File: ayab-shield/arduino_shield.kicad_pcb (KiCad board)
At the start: 2 copper layers, 73.1 x 53.3 mm, 36 parts, among them IC1 ULN2803A, IC2 ULN2803A, IC3 MCP2300X/P, IC4 MCP2300X/P, J1 Power, J2 Digital/PWM, J3 Analog, J4 Digital/PWM, X1 KLDX-0202-AC

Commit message: Gilding the lily
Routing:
- net GND: track 37.5 -> 16.6 mm, vias 2 -> 17
- net +15V: track 154.2 -> 138.8 mm
- net /SCL: track 111.9 -> 102.9 mm
- net /EOL_R: track 46.9 -> 39.5 mm
- net +5V: track 203.4 -> 198.6 mm, vias 0 -> 1
- net /ENC_A: track 25.9 -> 29.1 mm
- net /ENC_B: track 30.2 -> 28.3 mm
- net /SDA: track 95.1 -> 93.4 mm
- net /EOL_L: track 30.2 -> 29.2 mm

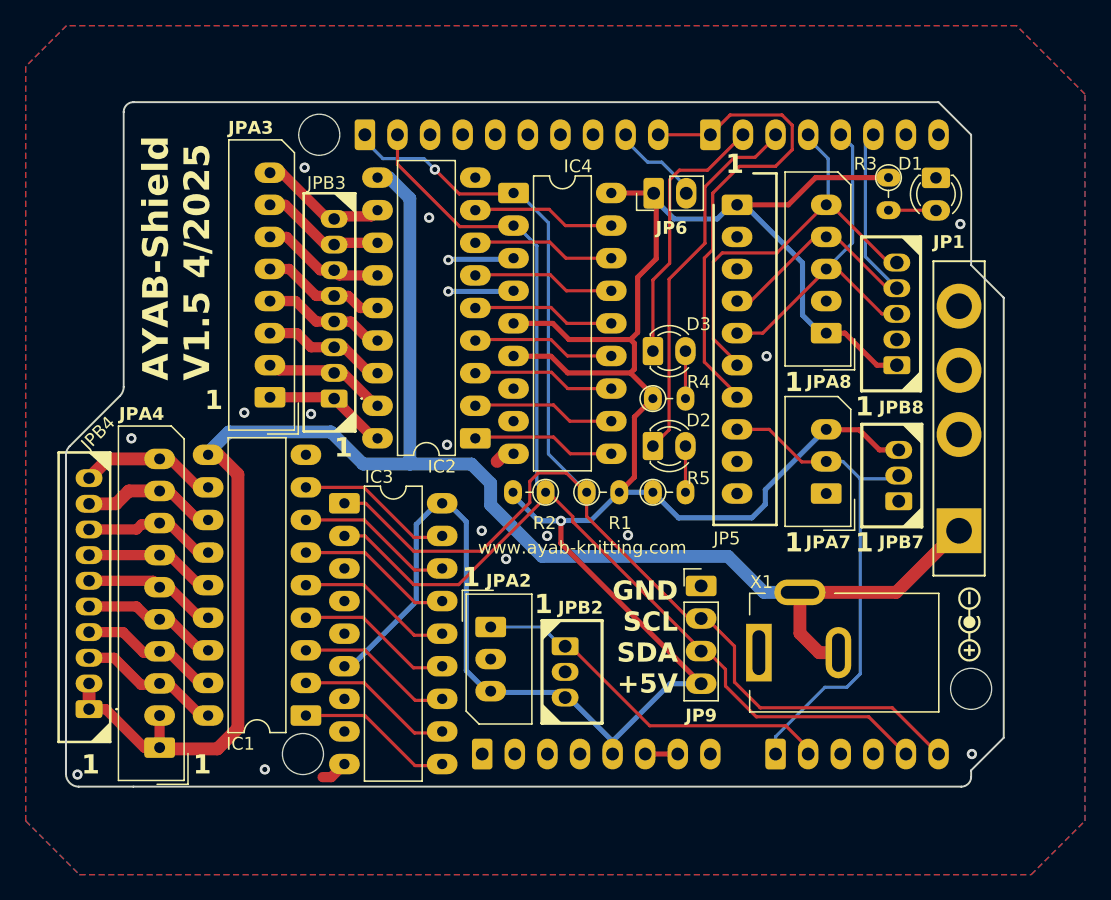
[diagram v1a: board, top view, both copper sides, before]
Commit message: Reverse pinout of JPB8
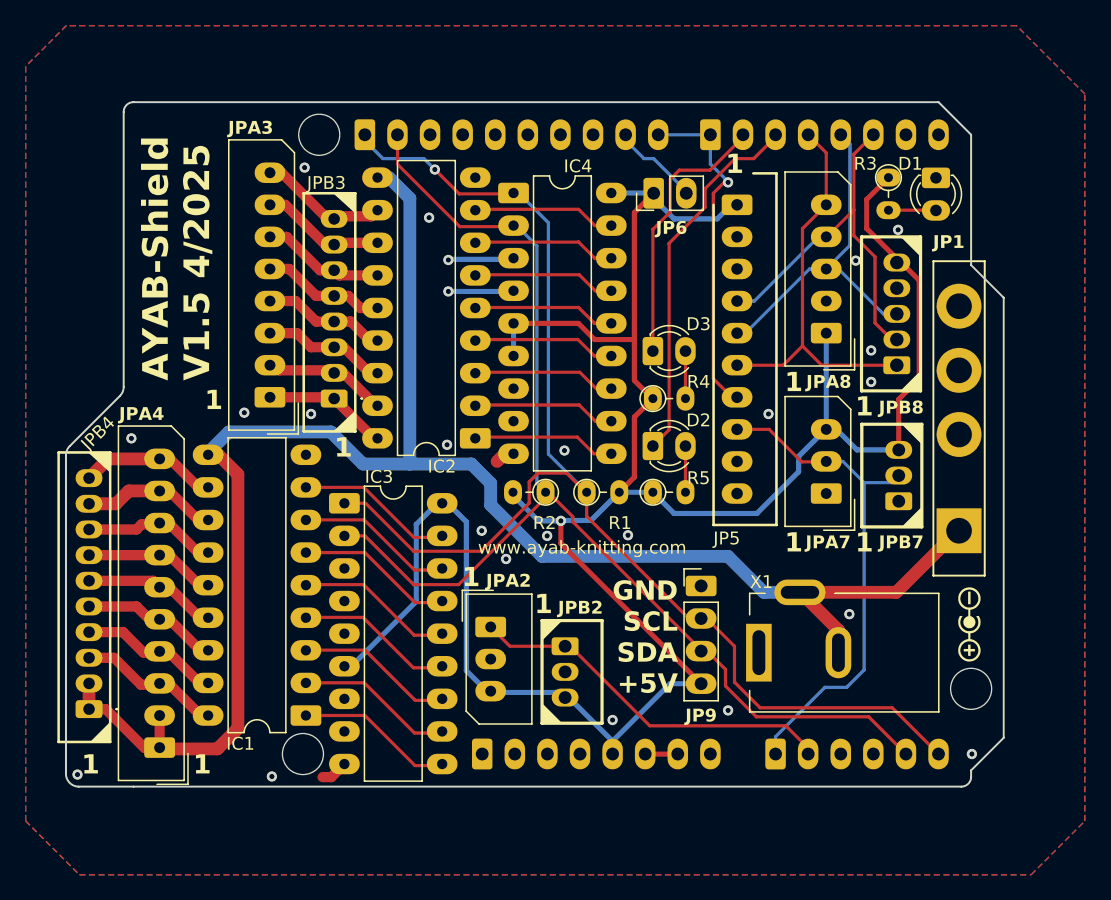
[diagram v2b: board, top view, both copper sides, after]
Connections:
- JPB8 pad 1: +5V -> /ENC_C
- JPB8 pad 2: GND -> /ENC_A
- JPB8 pad 4: /ENC_A -> GND
- JPB8 pad 5: /ENC_C -> +5V
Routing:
- net /910_L: track 38.2 -> 27.0 mm, vias 0 -> 1
- net +5V: track 198.6 -> 191.9 mm
- net /ENC_A: track 29.1 -> 30.3 mm
- net /ENC_C: track 32.9 -> 31.8 mm
- net +15V: track 138.8 -> 138.0 mm
- net GND: track 16.6 -> 17.4 mm, vias 17 -> 24
- net /ENC_B: track 28.3 -> 27.8 mm

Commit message: Remove JPB7
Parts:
- removed JPB7: 1X3 2mm, ayab-library:CONN-TH_3P-P2.00_A2004WV-3P
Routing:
- net +5V: track 191.9 -> 188.5 mm
- net /EOL_R: track 39.6 -> 36.6 mm
- net GND: vias 24 -> 25

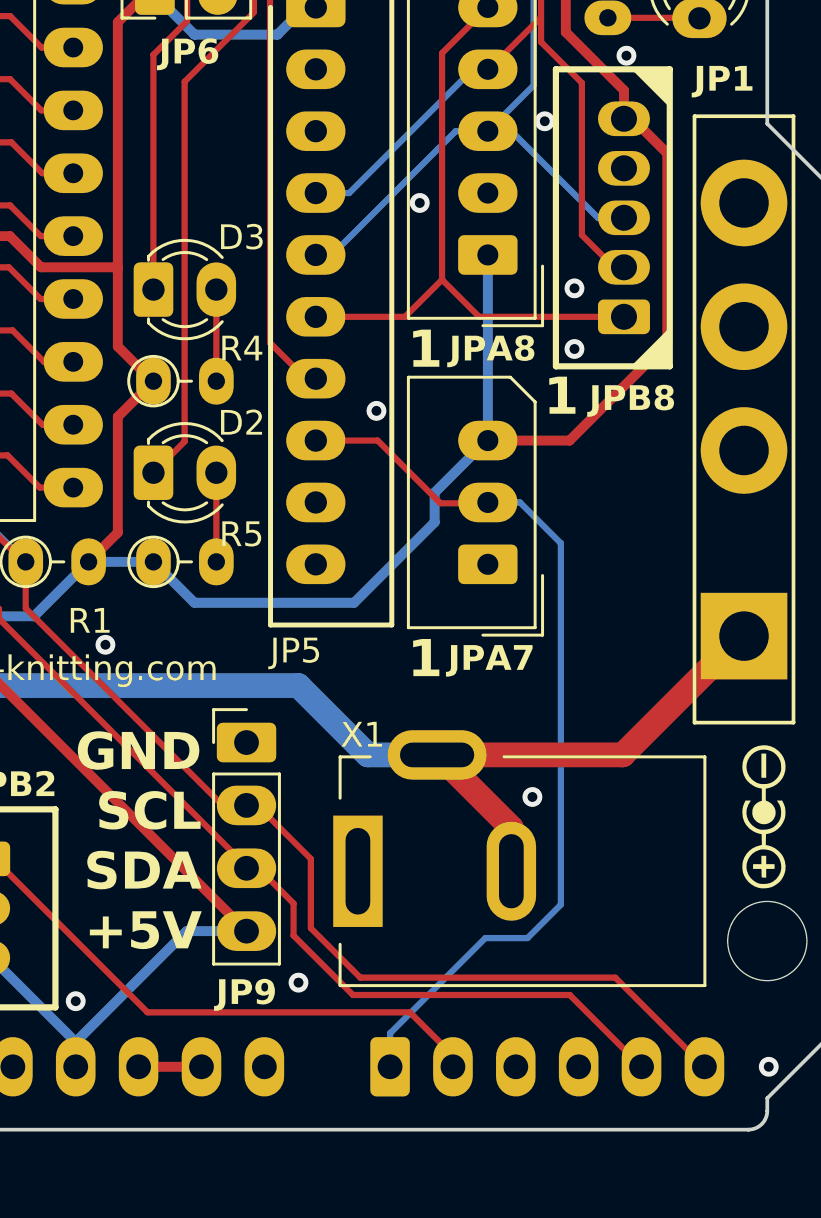
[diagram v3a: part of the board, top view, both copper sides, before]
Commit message: Fix pinout of JPA7
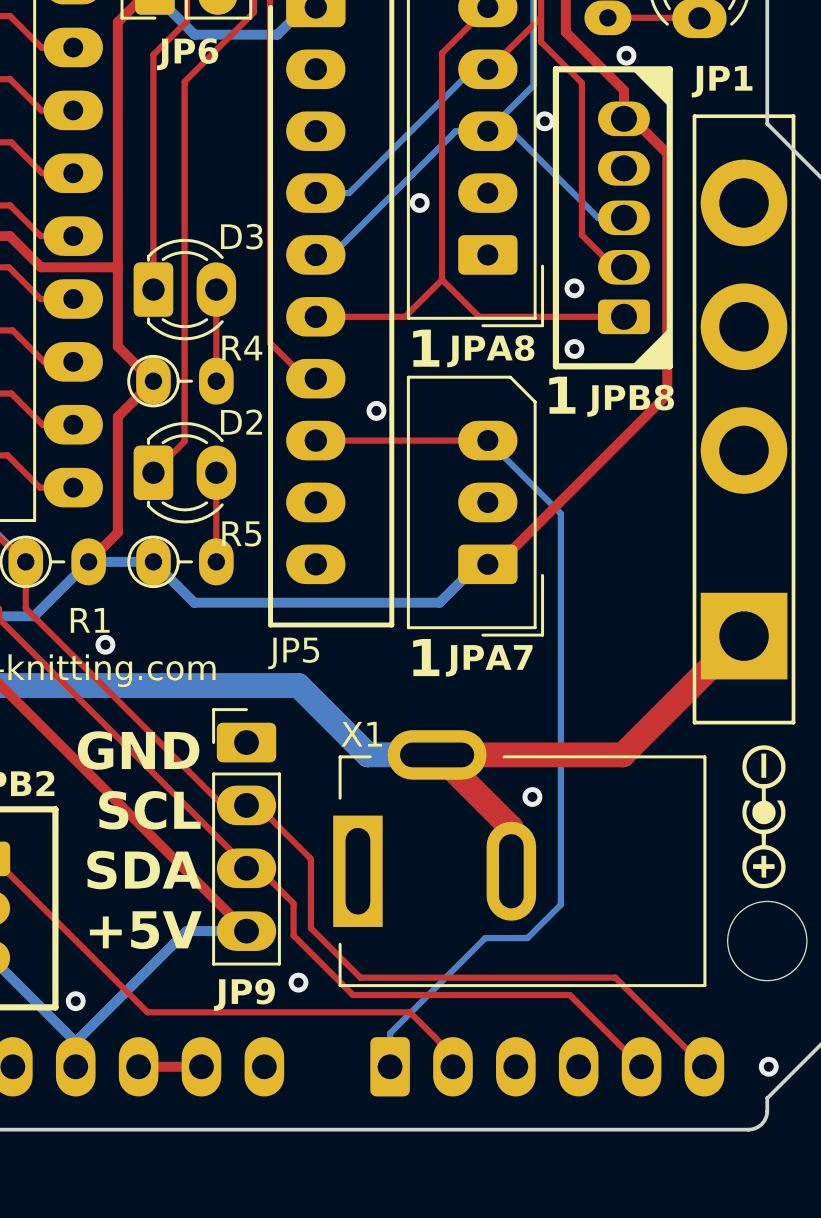
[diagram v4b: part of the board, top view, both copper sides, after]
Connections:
- JPA7 pad 1: GND -> +5V
- JPA7 pad 2: /EOL_R -> GND
- JPA7 pad 3: +5V -> /EOL_R
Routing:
- net +5V: track 188.5 -> 181.5 mm
- net /EOL_R: track 36.6 -> 37.3 mm
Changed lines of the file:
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@@
 			(remove_unused_layers no)
 			(roundrect_rratio 0.147059)
-			(net 2 "GND")
+			(net 3 "+5V")
 			(pinfunction "Pin_1")
 			(pintype "passive")
@@
 			(layers "*.Cu" "*.Mask")
 			(remove_unused_layers no)
-			(net 1 "/EOL_R")
+			(net 2 "GND")
 			(pinfunction "Pin_2")
 			(pintype "passive")
@@
 			(layers "*.Cu" "*.Mask")
 			(remove_unused_layers no)
-			(net 3 "+5V")
+			(net 1 "/EOL_R")
 			(pinfunction "Pin_3")
 			(pintype "passive")
@@
 	)
 	(segment
-		(start 167.5325 104.7325)
-		(end 169.5675 104.7325)
+		(start 162.7 102.2)
+		(end 169.45 102.2)
 		(width 0.25)
 		(layer "F.Cu")
 		(net 1)
+	)
+	(segment
+		(start 172.4 120.95)
+		(end 171.05 122.3)
+		(width 0.25)
+		(layer "B.Cu")
+		(net 1)
+	)
+	(segment
+		(start 169.45 102.2)
+		(end 172.4 105.15)
+		(width 0.25)
+		(layer "B.Cu")
+		(net 1)
+	)
+	(segment
+		(start 172.4 105.15)
+		(end 172.4 120.95)
+		(width 0.25)
+		(layer "B.Cu")
+		(net 1)
+	)
+	(segment
+		(start 169.35 122.3)
+		(end 165.5 126.15)
+		(width 0.25)
+		(layer "B.Cu")
+		(net 1)
+	)
+	(segment
+		(start 171.05 122.3)
+		(end 169.35 122.3)
+		(width 0.25)
+		(layer "B.Cu")
+		(net 1)
+	)
+	(segment
+		(start 169.55 102.2)
+		(end 169.45 102.2)
+		(width 0.4)
+		(layer "B.Cu")
+		(net 1)
+	)
+	(segment
+		(start 165.5 126.15)
+		(end 165.5 127.5)
+		(width 0.25)
+		(layer "B.Cu")
+		(net 1)
+	)
+	(segment
+		(start 169.4 102.2)
+		(end 169.45 102.2)
+		(width 0.4)
+		(layer "B.Cu")
+		(net 1)
+	)
+	(segment
+		(start 145.08 104.1)
+		(end 144.4 104.1)
+		(width 1)
+		(layer "F.Cu")
+		(net 2)
 	)
 	(segment
@@
 		(width 0.25)
 		(layer "F.Cu")
-		(net 1)
-	)
-	(segment
-		(start 165 102.2)
-		(end 167.5325 104.7325)
+		(net 2)
+	)
+	(segment
+		(start 155.34 127.5)
+		(end 157.88 127.5)
+		(width 0.4)
+		(layer "F.Cu")
+		(net 2)
+	)
+	(segment
+		(start 169.8 92.2)
+		(end 169.45 92.2)
 		(width 0.25)
 		(layer "F.Cu")
-		(net 1)
+		(net 2)
 	)
 	(segment
 		(start 169.5675 104.7325)
 		(end 169.6 104.7)
-		(width 0.25)
-		(layer "F.Cu")
-		(net 1)
-	)
-	(segment
-		(start 162.7 102.2)
-		(end 165 102.2)
-		(width 0.25)
-		(layer "F.Cu")
-		(net 1)
-	)
-	(segment
-		(start 169.45 104.7)
-		(end 170.75 104.7)
-		(width 0.25)
-		(layer "B.Cu")
-		(net 1)
-	)
-	(segment
-		(start 172.4 120.95)
-		(end 172.4 106.35)
-		(width 0.25)
-		(layer "B.Cu")
-		(net 1)
-	)
-	(segment
-		(start 170.75 104.7)
-		(end 172.4 106.35)
-		(width 0.25)
-		(layer "B.Cu")
-		(net 1)
-	)
-	(segment
-		(start 165.5 126.15)
-		(end 169.35 122.3)
-		(width 0.25)
-		(layer "B.Cu")
-		(net 1)
-	)
-	(segment
-		(start 171.05 122.3)
-		(end 172.4 120.95)
-		(width 0.25)
-		(layer "B.Cu")
-		(net 1)
-	)
-	(segment
-		(start 169.35 122.3)
-		(end 171.05 122.3)
-		(width 0.25)
-		(layer "B.Cu")
-		(net 1)
-	)
-	(segment
-		(start 165.5 127.5)
-		(end 165.5 126.15)
-		(width 0.25)
-		(layer "B.Cu")
-		(net 1)
-	)
-	(segment
-		(start 145.08 104.1)
-		(end 144.4 104.1)
-		(width 1)
-		(layer "F.Cu")
-		(net 2)
-	)
-	(segment
-		(start 155.34 127.5)
-		(end 157.88 127.5)
-		(width 0.4)
-		(layer "F.Cu")
-		(net 2)
-	)
-	(segment
-		(start 169.8 92.2)
-		(end 169.45 92.2)
 		(width 0.25)
 		(layer "F.Cu")
@@
 	)
 	(segment
-		(start 174.95 89.2)
-		(end 175.3 89.2)
-		(width 0.4)
-		(layer "F.Cu")
-		(net 3)
-	)
-	(segment
 		(start 145.08 93.94)
 		(end 150.14 93.94)
@@
 	)
 	(segment
-		(start 176.7 90.6)
-		(end 176.7 98.25)
+		(start 169.85 107.2)
+		(end 169.45 107.2)
 		(width 0.4)
 		(layer "F.Cu")
@@
 	)
 	(segment
-		(start 176.7 98.25)
-		(end 172.75 102.2)
+		(start 176.7 90.6)
+		(end 176.7 100.35)
 		(width 0.4)
 		(layer "F.Cu")
@@
 		(start 139.58 107.9)
 		(end 139.52 107.96)
+		(width 0.4)
+		(layer "F.Cu")
+		(net 3)
+	)
+	(segment
+		(start 176.7 100.35)
+		(end 169.85 107.2)
 		(width 0.4)
 		(layer "F.Cu")
@@
 	)
 	(segment
-		(start 172.75 102.2)
-		(end 169.45 102.2)
+		(start 174.95 89.2)
+		(end 175.3 89.2)
 		(width 0.4)
 		(layer "F.Cu")
@@
 	)
 	(segment
+		(start 167.5 108.75)
+		(end 157.59 108.75)
+		(width 0.4)
+		(layer "B.Cu")
+		(net 3)
+	)
+	(segment
 		(start 148.771005 109.328995)
 		(end 148.8 109.3)
@@
 	)
 	(segment
-		(start 167.3 104.3)
-		(end 169.4 102.2)
+		(start 157.59 108.75)
+		(end 155.94 107.1)
 		(width 0.4)
 		(layer "B.Cu")
@@
 	)
 	(segment
-		(start 157.59 108.75)
-		(end 164.05 108.75)
-		(width 0.4)
-		(layer "B.Cu")
-		(net 3)
-	)
-	(segment
 		(start 155.94 107.1)
 		(end 153.32 107.1)
@@
 	)
 	(segment
-		(start 167.3 105.5)
-		(end 167.3 104.3)
-		(width 0.4)
-		(layer "B.Cu")
-		(net 3)
-	)
-	(segment
 		(start 143.3 122.6)
 		(end 143 122.6)
@@
 		(start 152.8 127.5)
 		(end 152.8 126.5)
-		(width 0.4)
-		(layer "B.Cu")
-		(net 3)
-	)
-	(segment
-		(start 164.05 108.75)
-		(end 167.3 105.5)
 		(width 0.4)
 		(layer "B.Cu")
@@
 	)
 	(segment
-		(start 169.45 102.2)
-		(end 169.45 94.7)
-		(width 0.4)
-		(layer "B.Cu")
-		(net 3)
-	)
-	(segment
 		(start 152.8 126.5)
 		(end 157.28 122.02)
@@
 	)
 	(segment
+		(start 169.05 107.2)
+		(end 167.5 108.75)
+		(width 0.4)
+		(layer "B.Cu")
+		(net 3)
+	)
+	(segment
 		(start 143.35 122.7)
 		(end 148.4 122.7)
@@
 		(start 147.028995 109.328995)
 		(end 145.04 107.34)
-		(width 0.4)
-		(layer "B.Cu")
-		(net 3)
-	)
-	(segment
-		(start 155.94 107.1)
-		(end 157.59 108.75)
-		(width 0.4)
-		(layer "B.Cu")
-		(net 3)
-	)
-	(segment
-		(start 169.55 102.2)
-		(end 169.45 102.2)
 		(width 0.4)
 		(layer "B.Cu")
@@
 	)
 	(segment
-		(start 169.4 102.2)
-		(end 169.45 102.2)
-		(width 0.4)
-		(layer "B.Cu")
-		(net 3)
-	)
-	(segment
 		(start 151.12 109.3)
 		(end 153.32 107.1)
 		(width 0.4)
 		(layer "B.Cu")
+		(net 3)
+	)
+	(segment
+		(start 169.45 107.2)
+		(end 169.05 107.2)
+		(width 0.4)
+		(layer "B.Cu")

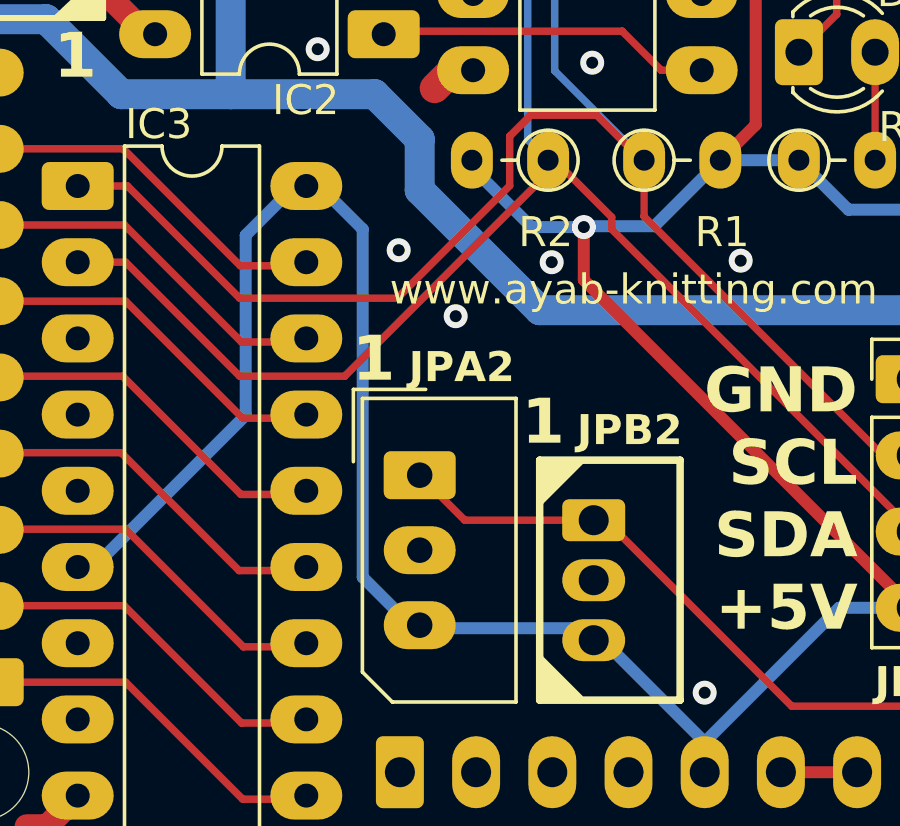
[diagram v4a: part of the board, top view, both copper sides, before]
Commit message: Fix pinout of JPA2
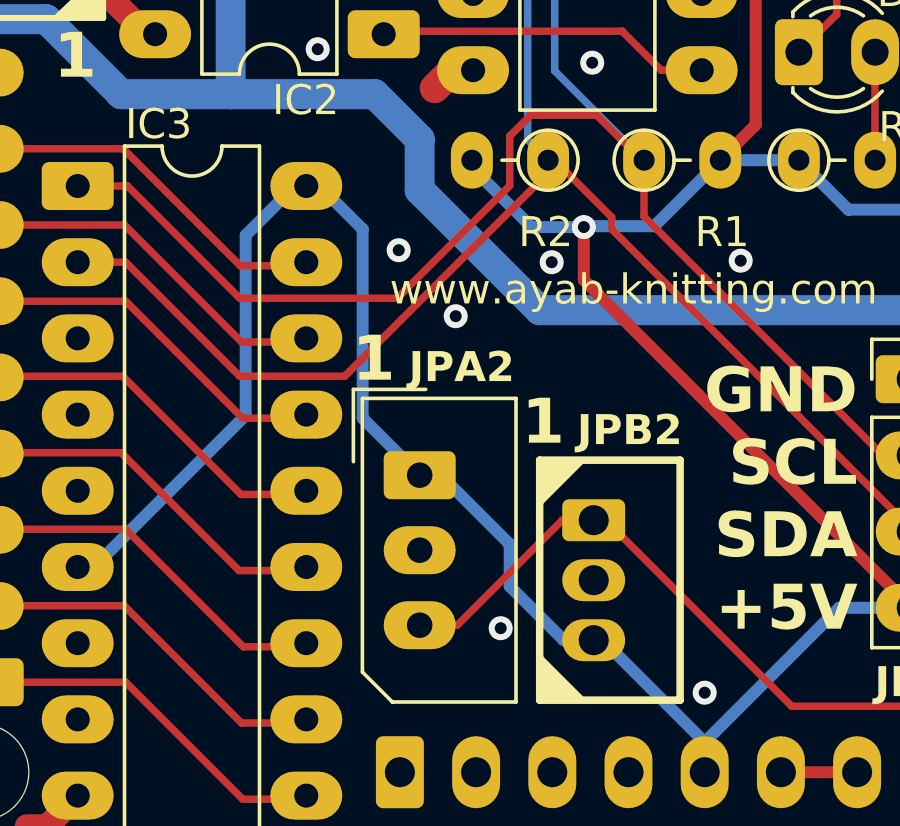
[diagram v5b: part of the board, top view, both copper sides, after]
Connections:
- JPA2 pad 1: /EOL_L -> +5V
- JPA2 pad 3: +5V -> /EOL_L
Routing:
- net +5V: track 181.5 -> 179.5 mm
- net /EOL_L: track 29.2 -> 30.4 mm
- net GND: vias 25 -> 26
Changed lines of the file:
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@@
 			(remove_unused_layers no)
 			(roundrect_rratio 0.147059)
-			(net 5 "/EOL_L")
+			(net 3 "+5V")
 			(pinfunction "Pin_1")
 			(pintype "passive")
@@
 			(layers "*.Cu" "*.Mask")
 			(remove_unused_layers no)
-			(net 3 "+5V")
+			(net 5 "/EOL_L")
 			(pinfunction "Pin_3")
 			(pintype "passive")
@@
 	)
 	(via
+		(at 146 122.7)
+		(size 0.8)
+		(drill 0.4)
+		(layers "F.Cu" "B.Cu")
+		(free yes)
+		(net 2)
+	)
+	(via
 		(at 129.3 101)
 		(size 0.8)
@@
 	)
 	(segment
-		(start 143.25 122.6)
-		(end 143.35 122.7)
-		(width 0.4)
-		(layer "F.Cu")
-		(net 3)
-	)
-	(segment
 		(start 154.5 101.24)
 		(end 155.94 99.8)
@@
 	)
 	(segment
-		(start 148.4 122.7)
-		(end 148.8 123.1)
+		(start 141.4 109.4)
+		(end 141.4 115.7)
 		(width 0.4)
 		(layer "B.Cu")
@@
 	)
 	(segment
-		(start 143.3 122.6)
-		(end 143 122.6)
-		(width 0.4)
-		(layer "B.Cu")
-		(net 3)
-	)
-	(segment
 		(start 137.5 115.6)
 		(end 132.44 120.66)
@@
 	)
 	(segment
+		(start 141.4 115.7)
+		(end 143.3 117.6)
+		(width 0.4)
+		(layer "B.Cu")
+		(net 3)
+	)
+	(segment
 		(start 152.8 127.5)
 		(end 152.8 126.5)
@@
 	)
 	(segment
+		(start 146.3 119.9)
+		(end 144 117.6)
+		(width 0.4)
+		(layer "B.Cu")
+		(net 3)
+	)
+	(segment
 		(start 174.95 89.2)
 		(end 174.8 89.2)
@@
 	)
 	(segment
-		(start 143 122.6)
-		(end 141.4 121)
+		(start 149.1 123.1)
+		(end 148.1 123.1)
 		(width 0.4)
 		(layer "B.Cu")
@@
 	)
 	(segment
-		(start 152.8 126.5)
-		(end 157.28 122.02)
+		(start 139.96 107.96)
+		(end 141.4 109.4)
 		(width 0.4)
 		(layer "B.Cu")
@@
 	)
 	(segment
-		(start 141.4 109.4)
-		(end 139.96 107.96)
+		(start 144 117.6)
+		(end 143.3 117.6)
+		(width 0.4)
+		(layer "B.Cu")
+		(net 3)
+	)
+	(segment
+		(start 152.8 126.5)
+		(end 157.28 122.02)
 		(width 0.4)
 		(layer "B.Cu")
@@
 	)
 	(segment
-		(start 162.05 84.7)
-		(end 162.5 84.7)
+		(start 148.1 123.1)
+		(end 146.3 121.3)
 		(width 0.4)
 		(layer "B.Cu")
@@
 	)
 	(segment
-		(start 169.05 107.2)
-		(end 167.5 108.75)
+		(start 162.05 84.7)
+		(end 162.5 84.7)
 		(width 0.4)
 		(layer "B.Cu")
@@
 	)
 	(segment
-		(start 143.35 122.7)
-		(end 148.4 122.7)
+		(start 169.05 107.2)
+		(end 167.5 108.75)
 		(width 0.4)
 		(layer "B.Cu")
@@
 	)
 	(segment
-		(start 141.4 121)
-		(end 141.4 109.4)
+		(start 143.3 117.6)
+		(end 143.25 117.6)
+		(width 0.25)
+		(layer "B.Cu")
+		(net 3)
+	)
+	(segment
+		(start 139.52 107.96)
+		(end 139.96 107.96)
 		(width 0.4)
 		(layer "B.Cu")
@@
 	)
 	(segment
-		(start 139.96 107.96)
-		(end 139.52 107.96)
+		(start 146.3 121.3)
+		(end 146.3 119.9)
 		(width 0.4)
 		(layer "B.Cu")
@@
 	)
 	(segment
-		(start 148.8 119.1)
-		(end 144.8 119.1)
+		(start 143.3 122.6)
+		(end 144.55 122.6)
 		(width 0.25)
 		(layer "F.Cu")
@@
 	)
 	(segment
-		(start 144.8 119.1)
-		(end 143.3 117.6)
-		(width 0.25)
+		(start 143.25 122.6)
+		(end 143.35 122.7)
+		(width 0.4)
 		(layer "F.Cu")
 		(net 5)
@@
 	)
 	(segment
+		(start 144.55 122.6)
+		(end 148.05 119.1)
+		(width 0.25)
+		(layer "F.Cu")
+		(net 5)
+	)
+	(segment
 		(start 149.5 119.1)
 		(end 148.8 119.1)
@@
 	)
 	(segment
-		(start 143.3 117.6)
-		(end 143.25 117.6)
+		(start 148.05 119.1)
+		(end 149.1 119.1)
 		(width 0.25)
-		(layer "B.Cu")
+		(layer "F.Cu")
 		(net 5)
 	)
